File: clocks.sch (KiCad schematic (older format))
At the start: 10 parts, among them U13 Si5351A-B-GT, U4 5M1270ZT144C5N, X1 CB3LV-3I-50M0000, Y2 25MHZ 8PF

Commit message: component placement
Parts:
- U4: symbol CPLD_Altera:5M1270ZT144C5N -> rc2014_max_v-rescue:5M1270ZT144C5N-CPLD_Altera
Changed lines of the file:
@@
 IO1_CLK0
 $Comp
-L CPLD_Altera:5M1270ZT144C5N U?
+L rc2014_max_v-rescue:5M1270ZT144C5N-CPLD_Altera U?
 U 5 1 5D0055D3
 P 5480 3000
@@
 AR Path="/5CFABACD/5D0055D3" Ref="U?"  Part="5"
 AR Path="/5CFABACD/5CFFC458/5D0055D3" Ref="U4"  Part="5"
+AR Path="/5D0055D3" Ref="U4"  Part="5"
 F 0 "U4" H 5838 2838 50  0000 L CNN
 F 1 "5M1270ZT144C5N" H 5838 2747 50  0000 L CNN

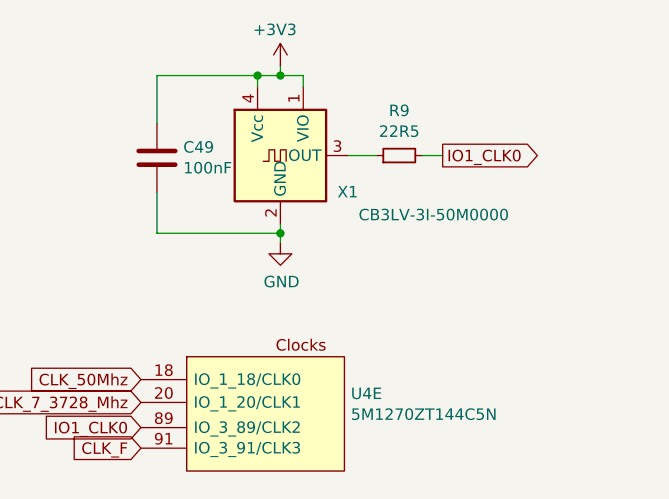
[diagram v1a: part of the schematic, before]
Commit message: updated clock
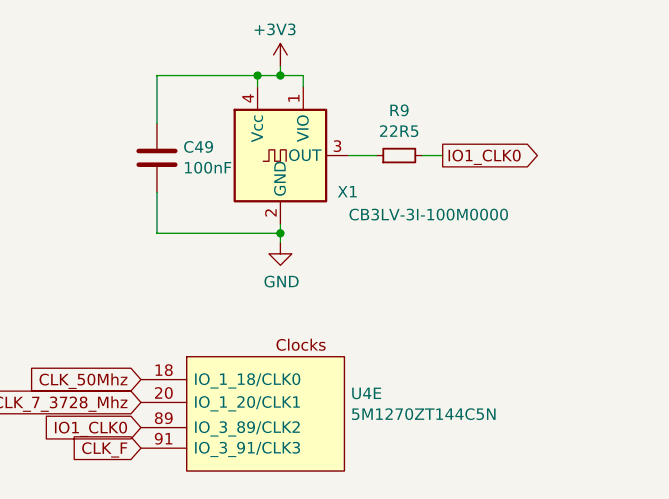
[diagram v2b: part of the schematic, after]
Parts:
- X1: value CB3LV-3I-50M0000 -> CB3LV-3I-100M0000
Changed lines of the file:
@@
 AR Path="/5CFABACD/5CFFC458/5D005597" Ref="X1"  Part="1"
 F 0 "X1" H 5870 1960 50  0000 R CNN
-F 1 "CB3LV-3I-50M0000" H 6530 1860 50  0000 R CNN
+F 1 "CB3LV-3I-100M0000" H 6530 1860 50  0000 R CNN
 F 2 "Oscillator:Oscillator_SMD_SeikoEpson_SG8002CA-4Pin_7.0x5.0mm_HandSoldering" H 5530 1770 50  0001 C CNN
 F 3 "https://www.mouser.com/datasheet/2/96/008-0256-0-786323.pdf" H 5430 2120 50  0001 C CNN

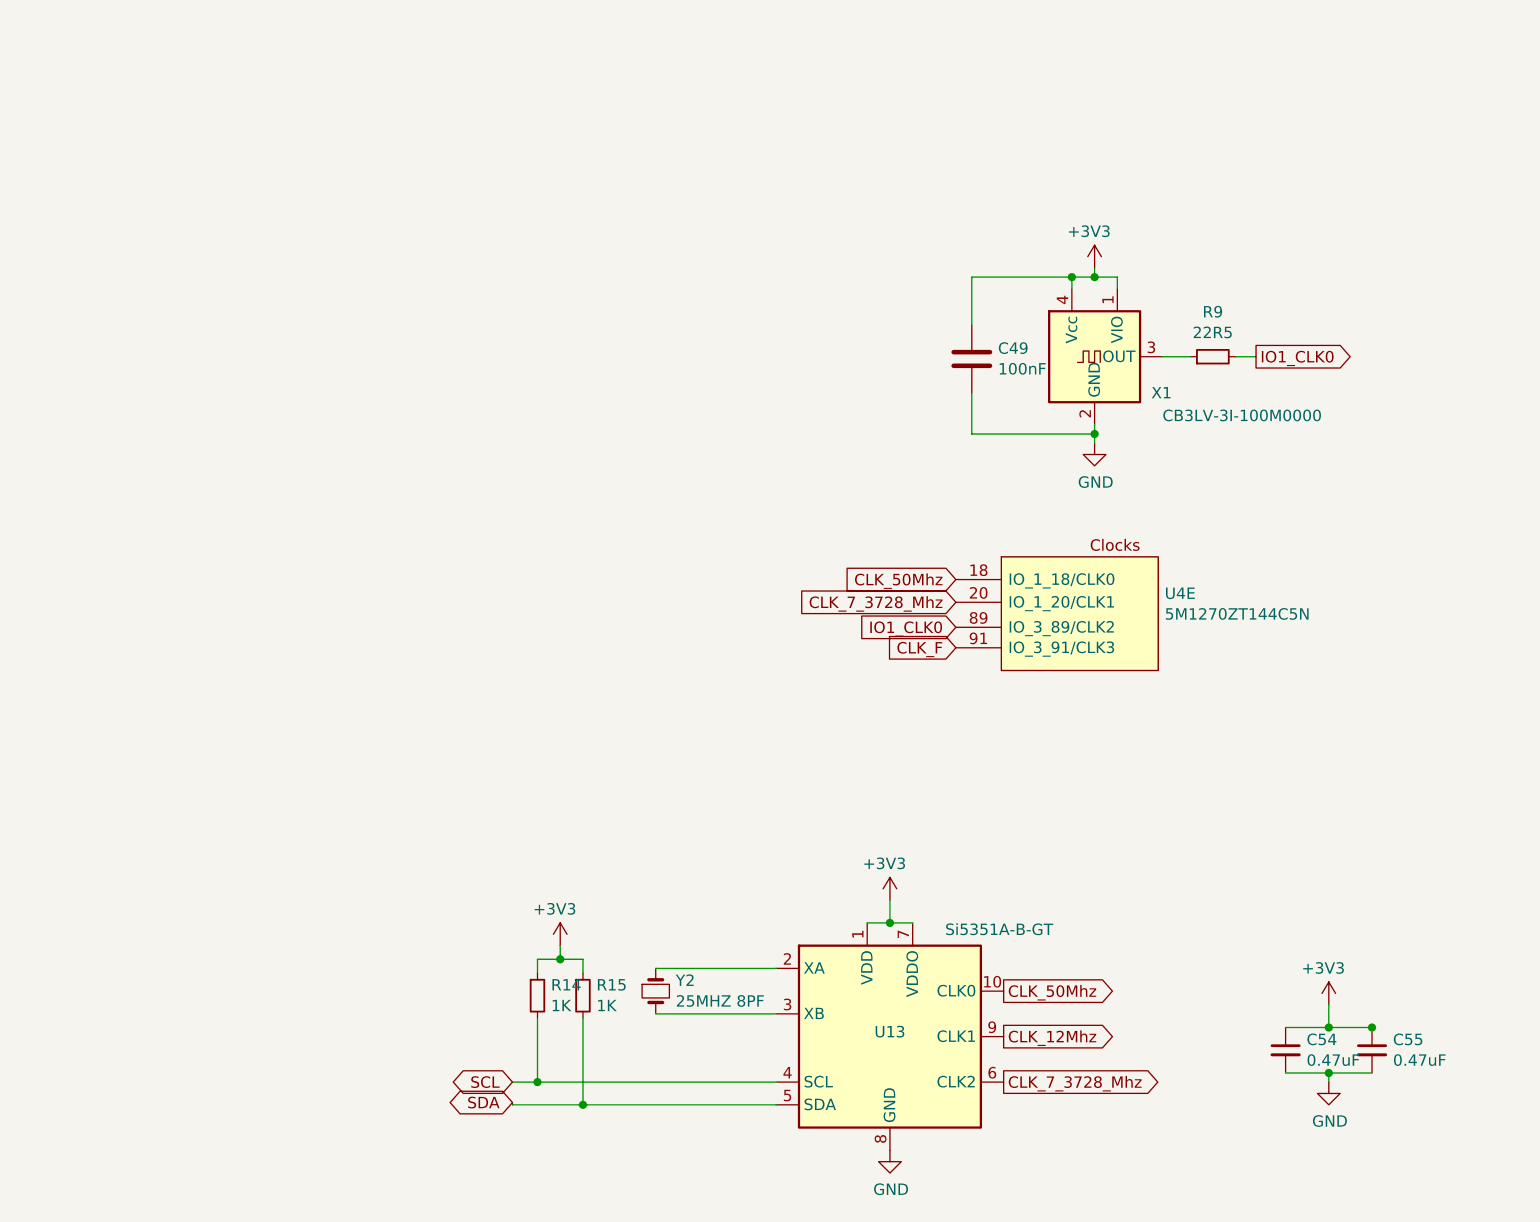
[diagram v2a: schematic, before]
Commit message: organized bypass caps
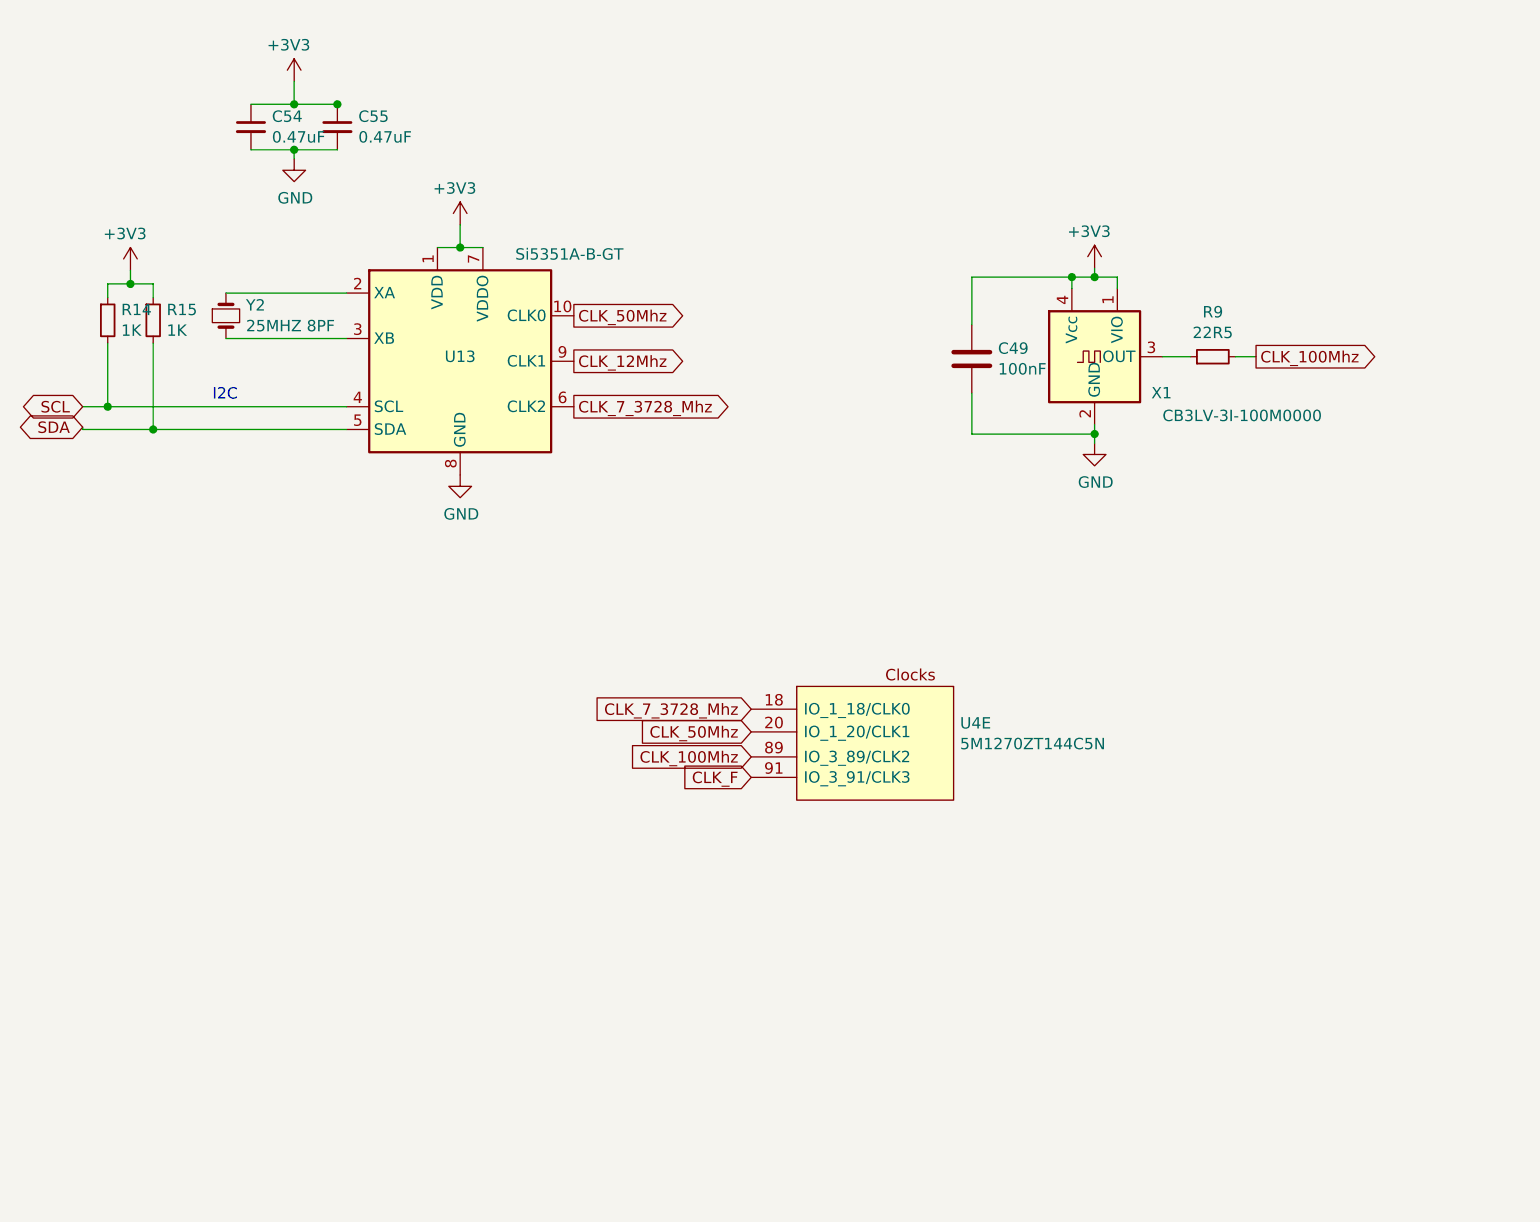
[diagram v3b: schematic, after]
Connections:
- net labels added: CLK_100Mhz
- net labels removed: IO1_CLK0
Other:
- note added: "I2C"
- moved on the sheet: C54, C55, R14, R15, U13, U4E, Y2

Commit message: fixed errors, connected all pins, switched to 4 layers
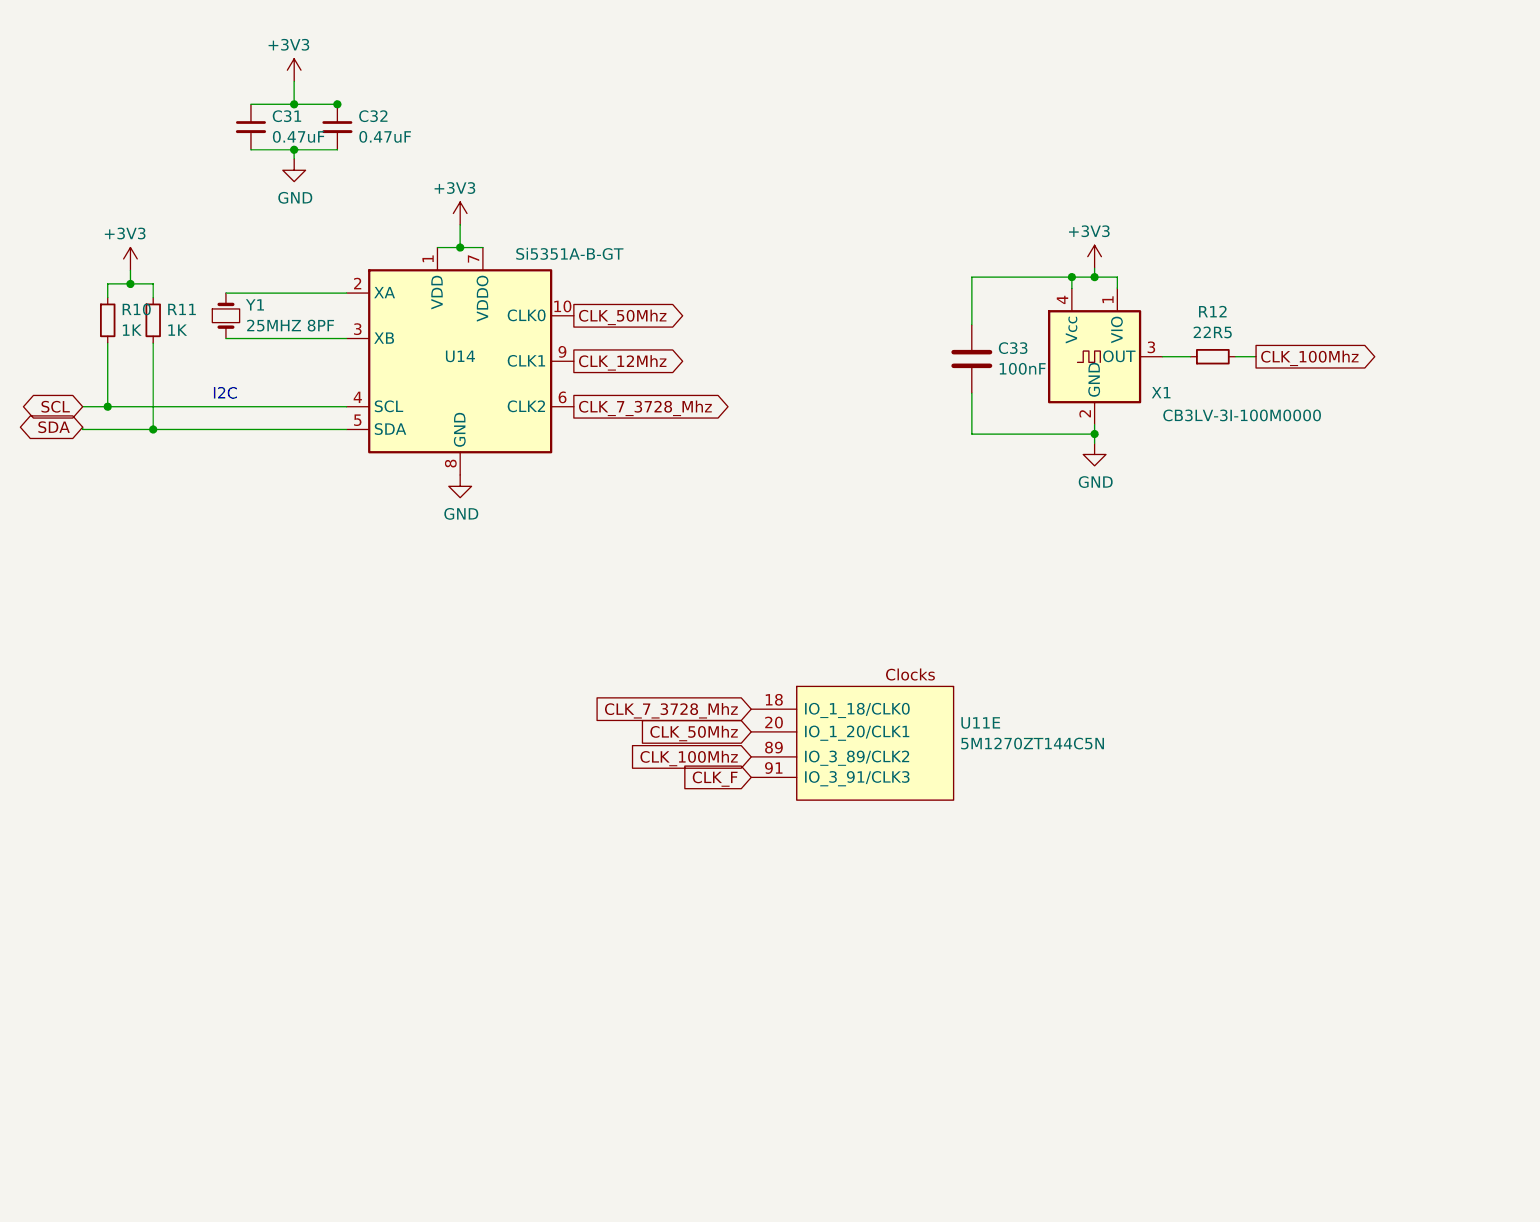
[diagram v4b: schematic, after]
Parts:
- renumbered C54 to C31, C55 to C32, C49 to C33, R14 to R10, R15 to R11, R9 to R12, U4 to U11, U13 to U14, Y2 to Y1
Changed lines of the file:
@@
 AR Path="/5D0F9837/5D0055A1" Ref="#PWR?"  Part="1"
 AR Path="/5CFABACD/5D0055A1" Ref="#PWR?"  Part="1"
-AR Path="/5CFABACD/5CFFC458/5D0055A1" Ref="#PWR060"  Part="1"
-F 0 "#PWR060" H 5530 2250 50  0001 C CNN
+AR Path="/5CFABACD/5CFFC458/5D0055A1" Ref="#PWR065"  Part="1"
+F 0 "#PWR065" H 5530 2250 50  0001 C CNN
 F 1 "GND" H 5535 2327 50  0000 C CNN
 F 2 "" H 5530 2500 50  0001 C CNN
@@
 AR Path="/5D0F9837/5D0055A7" Ref="#PWR?"  Part="1"
 AR Path="/5CFABACD/5D0055A7" Ref="#PWR?"  Part="1"
-AR Path="/5CFABACD/5CFFC458/5D0055A7" Ref="#PWR059"  Part="1"
-F 0 "#PWR059" H 5530 1580 50  0001 C CNN
+AR Path="/5CFABACD/5CFFC458/5D0055A7" Ref="#PWR063"  Part="1"
+F 0 "#PWR063" H 5530 1580 50  0001 C CNN
 F 1 "+3V3" H 5410 1890 50  0000 L CNN
 F 2 "" H 5530 1730 50  0001 C CNN
@@
 AR Path="/5D0F9837/5D0055B0" Ref="R?"  Part="1"
 AR Path="/5CFABACD/5D0055B0" Ref="R?"  Part="1"
-AR Path="/5CFABACD/5CFFC458/5D0055B0" Ref="R9"  Part="1"
-F 0 "R9" V 6246 2120 50  0000 C CNN
+AR Path="/5CFABACD/5CFFC458/5D0055B0" Ref="R12"  Part="1"
+F 0 "R12" V 6246 2120 50  0000 C CNN
 F 1 "22R5" V 6155 2120 50  0000 C CNN
 F 2 "Resistor_SMD:R_0603_1608Metric_Pad1.05x0.95mm_HandSolder" H 6050 2120 50  0001 C CNN
@@
 AR Path="/5D0055BE" Ref="C?"  Part="1"
 AR Path="/5D0F9837/5D0055BE" Ref="C?"  Part="1"
-AR Path="/5CFABACD/5CFFC458/5D0055BE" Ref="C49"  Part="1"
-F 0 "C49" H 5105 2176 50  0000 L CNN
+AR Path="/5CFABACD/5CFFC458/5D0055BE" Ref="C33"  Part="1"
+F 0 "C33" H 5105 2176 50  0000 L CNN
 F 1 "100nF" H 5105 2085 50  0000 L CNN
 F 2 "Capacitor_SMD:C_0603_1608Metric_Pad1.05x0.95mm_HandSolder" H 5028 1980 50  0001 C CNN
@@
 AR Path="/5D0F9837/5D0055D3" Ref="U?"  Part="5"
 AR Path="/5CFABACD/5D0055D3" Ref="U?"  Part="5"
-AR Path="/5CFABACD/5CFFC458/5D0055D3" Ref="U4"  Part="5"
-AR Path="/5D0055D3" Ref="U4"  Part="5"
-F 0 "U4" H 4938 3408 50  0000 L CNN
+AR Path="/5CFABACD/5CFFC458/5D0055D3" Ref="U11"  Part="5"
+AR Path="/5D0055D3" Ref="U?"  Part="5"
+F 0 "U11" H 4938 3408 50  0000 L CNN
 F 1 "5M1270ZT144C5N" H 4938 3317 50  0000 L CNN
 F 2 "Package_QFP:TQFP-144_20x20mm_P0.5mm" H 6420 6470 50  0001 L CNN
@@
 F 4 "CPLD - Complex Programmable Logic Devices CPLD - MAX V 980 Macro 114 IOs" H 6420 6270 50  0001 L CNN "Description"
 F 5 "1.55" H 6420 6170 50  0001 L CNN "Height"
-F 6 "" H 6420 6070 50  0001 L CNN "Mouser Part Number"
-F 7 "" H 6420 5970 50  0001 L CNN "Mouser Price/Stock"
-F 8 "Intel" H 6420 5870 50  0001 L CNN "Manufacturer_Name"
-F 9 "5M1270ZT144C5N" H 6420 5770 50  0001 L CNN "Manufacturer_Part_Number"
+F 6 "Intel" H 6420 5870 50  0001 L CNN "Manufacturer_Name"
+F 7 "5M1270ZT144C5N" H 6420 5770 50  0001 L CNN "Manufacturer_Part_Number"
 	5    4580 3570
 	1    0    0    -1
@@
 P 2740 2140
 AR Path="/5CFABACD/5D0055D9" Ref="U?"  Part="1"
-AR Path="/5CFABACD/5CFFC458/5D0055D9" Ref="U13"  Part="1"
-F 0 "U13" H 2740 2160 50  0000 C CNN
+AR Path="/5CFABACD/5CFFC458/5D0055D9" Ref="U14"  Part="1"
+F 0 "U14" H 2740 2160 50  0000 C CNN
 F 1 "Si5351A-B-GT" H 3220 2610 50  0000 C CNN
 F 2 "Package_SO:MSOP-10_3x3mm_P0.5mm" H 2740 1340 50  0001 C CNN
@@
 $EndComp
 $Comp
-L Device:Crystal_Small Y2
+L Device:Crystal_Small Y1
 U 1 1 5D00617A
 P 1710 1940
-F 0 "Y2" V 1664 2028 50  0000 L CNN
+F 0 "Y1" V 1664 2028 50  0000 L CNN
 F 1 "25MHZ 8PF" V 1755 2028 50  0000 L CNN
 F 2 "Crystal:Crystal_SMD_TXC_7A-2Pin_5x3.2mm" H 1710 1940 50  0001 C CNN
@@
 AR Path="/5D0F9837/5D00A003" Ref="#PWR?"  Part="1"
 AR Path="/5CFABACD/5D00A003" Ref="#PWR?"  Part="1"
-AR Path="/5CFABACD/5CFFC458/5D00A003" Ref="#PWR088"  Part="1"
-F 0 "#PWR088" H 2740 2390 50  0001 C CNN
+AR Path="/5CFABACD/5CFFC458/5D00A003" Ref="#PWR066"  Part="1"
+F 0 "#PWR066" H 2740 2390 50  0001 C CNN
 F 1 "GND" H 2745 2467 50  0000 C CNN
 F 2 "" H 2740 2640 50  0001 C CNN
@@
 AR Path="/5D0F9837/5D00B94C" Ref="#PWR?"  Part="1"
 AR Path="/5CFABACD/5D00B94C" Ref="#PWR?"  Part="1"
-AR Path="/5CFABACD/5CFFC458/5D00B94C" Ref="#PWR063"  Part="1"
-F 0 "#PWR063" H 2740 1390 50  0001 C CNN
+AR Path="/5CFABACD/5CFFC458/5D00B94C" Ref="#PWR062"  Part="1"
+F 0 "#PWR062" H 2740 1390 50  0001 C CNN
 F 1 "+3V3" H 2620 1700 50  0000 L CNN
 F 2 "" H 2740 1540 50  0001 C CNN
@@
 $EndComp
 $Comp
-L Device:C_Small C54
+L Device:C_Small C31
 U 1 1 5D00C0F7
 P 1820 1110
-F 0 "C54" H 1912 1156 50  0000 L CNN
+F 0 "C31" H 1912 1156 50  0000 L CNN
 F 1 "0.47uF" H 1912 1065 50  0000 L CNN
 F 2 "Capacitor_SMD:C_0603_1608Metric_Pad1.05x0.95mm_HandSolder" H 1820 1110 50  0001 C CNN
@@
 $EndComp
 $Comp
-L Device:C_Small C55
+L Device:C_Small C32
 U 1 1 5D00D019
 P 2200 1110
-F 0 "C55" H 2292 1156 50  0000 L CNN
+F 0 "C32" H 2292 1156 50  0000 L CNN
 F 1 "0.47uF" H 2292 1065 50  0000 L CNN
 F 2 "Capacitor_SMD:C_0603_1608Metric_Pad1.05x0.95mm_HandSolder" H 2200 1110 50  0001 C CNN
@@
 AR Path="/5D0F9837/5D00E3D9" Ref="#PWR?"  Part="1"
 AR Path="/5CFABACD/5D00E3D9" Ref="#PWR?"  Part="1"
-AR Path="/5CFABACD/5CFFC458/5D00E3D9" Ref="#PWR087"  Part="1"
-F 0 "#PWR087" H 2010 1000 50  0001 C CNN
+AR Path="/5CFABACD/5CFFC458/5D00E3D9" Ref="#PWR061"  Part="1"
+F 0 "#PWR061" H 2010 1000 50  0001 C CNN
 F 1 "GND" H 2015 1077 50  0000 C CNN
 F 2 "" H 2010 1250 50  0001 C CNN
@@
 AR Path="/5D0F9837/5D00F92A" Ref="#PWR?"  Part="1"
 AR Path="/5CFABACD/5D00F92A" Ref="#PWR?"  Part="1"
-AR Path="/5CFABACD/5CFFC458/5D00F92A" Ref="#PWR086"  Part="1"
-F 0 "#PWR086" H 2010 760 50  0001 C CNN
+AR Path="/5CFABACD/5CFFC458/5D00F92A" Ref="#PWR060"  Part="1"
+F 0 "#PWR060" H 2010 760 50  0001 C CNN
 F 1 "+3V3" H 1890 1070 50  0000 L CNN
 F 2 "" H 2010 910 50  0001 C CNN
@@
 SDA
 $Comp
-L Device:R_Small R14
+L Device:R_Small R10
 U 1 1 5D0168D6
 P 1190 1960
-F 0 "R14" H 1249 2006 50  0000 L CNN
+F 0 "R10" H 1249 2006 50  0000 L CNN
 F 1 "1K" H 1249 1915 50  0000 L CNN
 F 2 "Resistor_SMD:R_0603_1608Metric_Pad1.05x0.95mm_HandSolder" H 1190 1960 50  0001 C CNN
@@
 $EndComp
 $Comp
-L Device:R_Small R15
+L Device:R_Small R11
 U 1 1 5D017809
 P 1390 1960
-F 0 "R15" H 1449 2006 50  0000 L CNN
+F 0 "R11" H 1449 2006 50  0000 L CNN
 F 1 "1K" H 1449 1915 50  0000 L CNN
 F 2 "Resistor_SMD:R_0603_1608Metric_Pad1.05x0.95mm_HandSolder" H 1390 1960 50  0001 C CNN
@@
 AR Path="/5D0F9837/5D01ACA8" Ref="#PWR?"  Part="1"
 AR Path="/5CFABACD/5D01ACA8" Ref="#PWR?"  Part="1"
-AR Path="/5CFABACD/5CFFC458/5D01ACA8" Ref="#PWR066"  Part="1"
-F 0 "#PWR066" H 1290 1590 50  0001 C CNN
+AR Path="/5CFABACD/5CFFC458/5D01ACA8" Ref="#PWR064"  Part="1"
+F 0 "#PWR064" H 1290 1590 50  0001 C CNN
 F 1 "+3V3" H 1170 1900 50  0000 L CNN
 F 2 "" H 1290 1740 50  0001 C CNN
